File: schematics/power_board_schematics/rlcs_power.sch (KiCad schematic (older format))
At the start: 40 parts, among them J1 SD_Card, J2 Conn_01x05_Male, J3 Conn_01x05_Male, J4 Battery Conn, J5 CONN_01X02, J6 CONN_01X02, J7 CONN_01X02, Q1 Q_NPN_BEC, Q2 Q_NPN_BEC, T1 12 to 3v3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

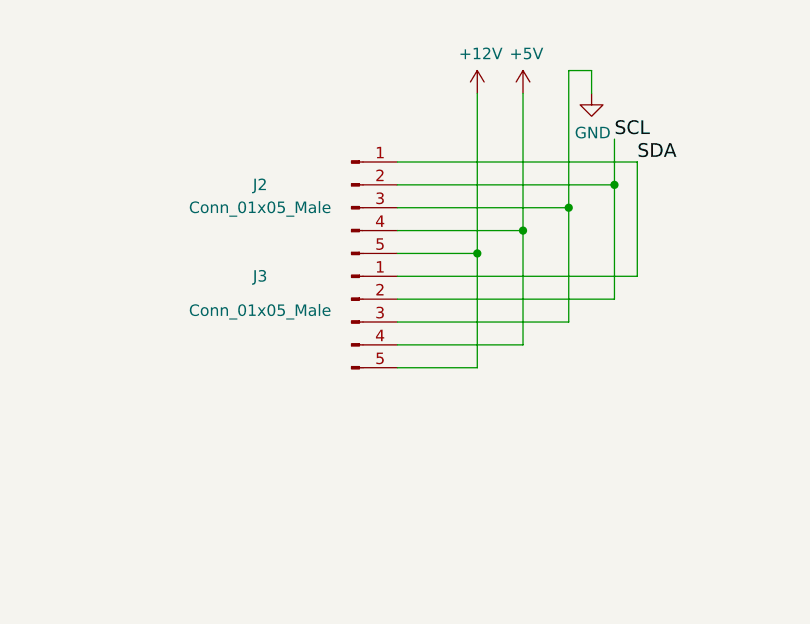
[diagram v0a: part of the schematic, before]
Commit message: Fix 7 segement display pins to make routing easier and fix footprints
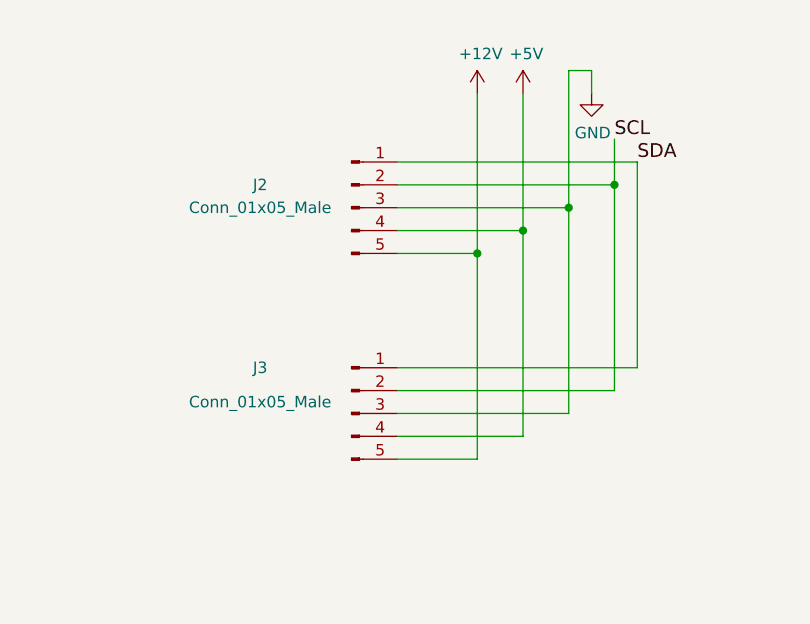
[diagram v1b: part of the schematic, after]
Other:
- moved on the sheet: J3
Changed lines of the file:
@@
 EESchema Schematic File Version 4
-LIBS:rlcs_power-cache
 EELAYER 30 0
 EELAYER END
@@
 Wire Wire Line
 	2650 5850 2500 5850
-Wire Wire Line
-	7750 4750 7750 5250
 Text Label 7750 4750 0    60   ~ 0
 SDA
@@
 Wire Wire Line
 	7550 4350 7550 4450
-Wire Wire Line
-	7650 4850 7650 5350
-Wire Wire Line
-	7750 5250 6700 5250
 Connection ~ 7450 4950
-Wire Wire Line
-	7450 4950 7450 5450
 Connection ~ 7250 5050
 Wire Wire Line
-	7250 5050 7250 5550
-Connection ~ 7050 5150
-Wire Wire Line
-	7050 5150 7050 5650
-Wire Wire Line
 	6700 4750 7750 4750
 Wire Wire Line
@@
 	7450 4350 7550 4350
 Wire Wire Line
-	7050 5650 6700 5650
-Wire Wire Line
-	7250 5550 6700 5550
-Wire Wire Line
-	7450 5450 6700 5450
-Wire Wire Line
-	7650 5350 6700 5350
+	7050 6050 6700 6050
+Wire Wire Line
+	7250 5950 6700 5950
+Wire Wire Line
+	7450 5850 6700 5850
+Wire Wire Line
+	7650 5750 6700 5750
 Connection ~ 7650 4850
 Wire Wire Line
@@
 L Connector:Conn_01x05_Male J3
 U 1 1 5EE7917B
-P 6500 5450
-F 0 "J3" H 6100 5650 50  0000 C CNN
-F 1 "Conn_01x05_Male" H 6100 5500 50  0000 C CNN
-F 2 "Connector_JST:JST_EH_B5B-EH-A_1x05_P2.50mm_Vertical" H 6500 5450 50  0001 C CNN
-F 3 "~" H 6500 5450 50  0001 C CNN
-	1    6500 5450
+P 6500 5850
+F 0 "J3" H 6100 6050 50  0000 C CNN
+F 1 "Conn_01x05_Male" H 6100 5900 50  0000 C CNN
+F 2 "Connector_JST:JST_EH_B5B-EH-A_1x05_P2.50mm_Vertical" H 6500 5850 50  0001 C CNN
+F 3 "~" H 6500 5850 50  0001 C CNN
+	1    6500 5850
 	1    0    0    -1
 $EndComp
@@
 	1    0    0    -1
 $EndComp
+Wire Wire Line
+	6700 5650 7750 5650
+Wire Wire Line
+	7050 5150 7050 6050
+Connection ~ 7050 5150
+Wire Wire Line
+	7250 5050 7250 5950
+Wire Wire Line
+	7450 4950 7450 5850
+Wire Wire Line
+	7650 4850 7650 5750
+Wire Wire Line
+	7750 4750 7750 5650
 $EndSCHEMATC

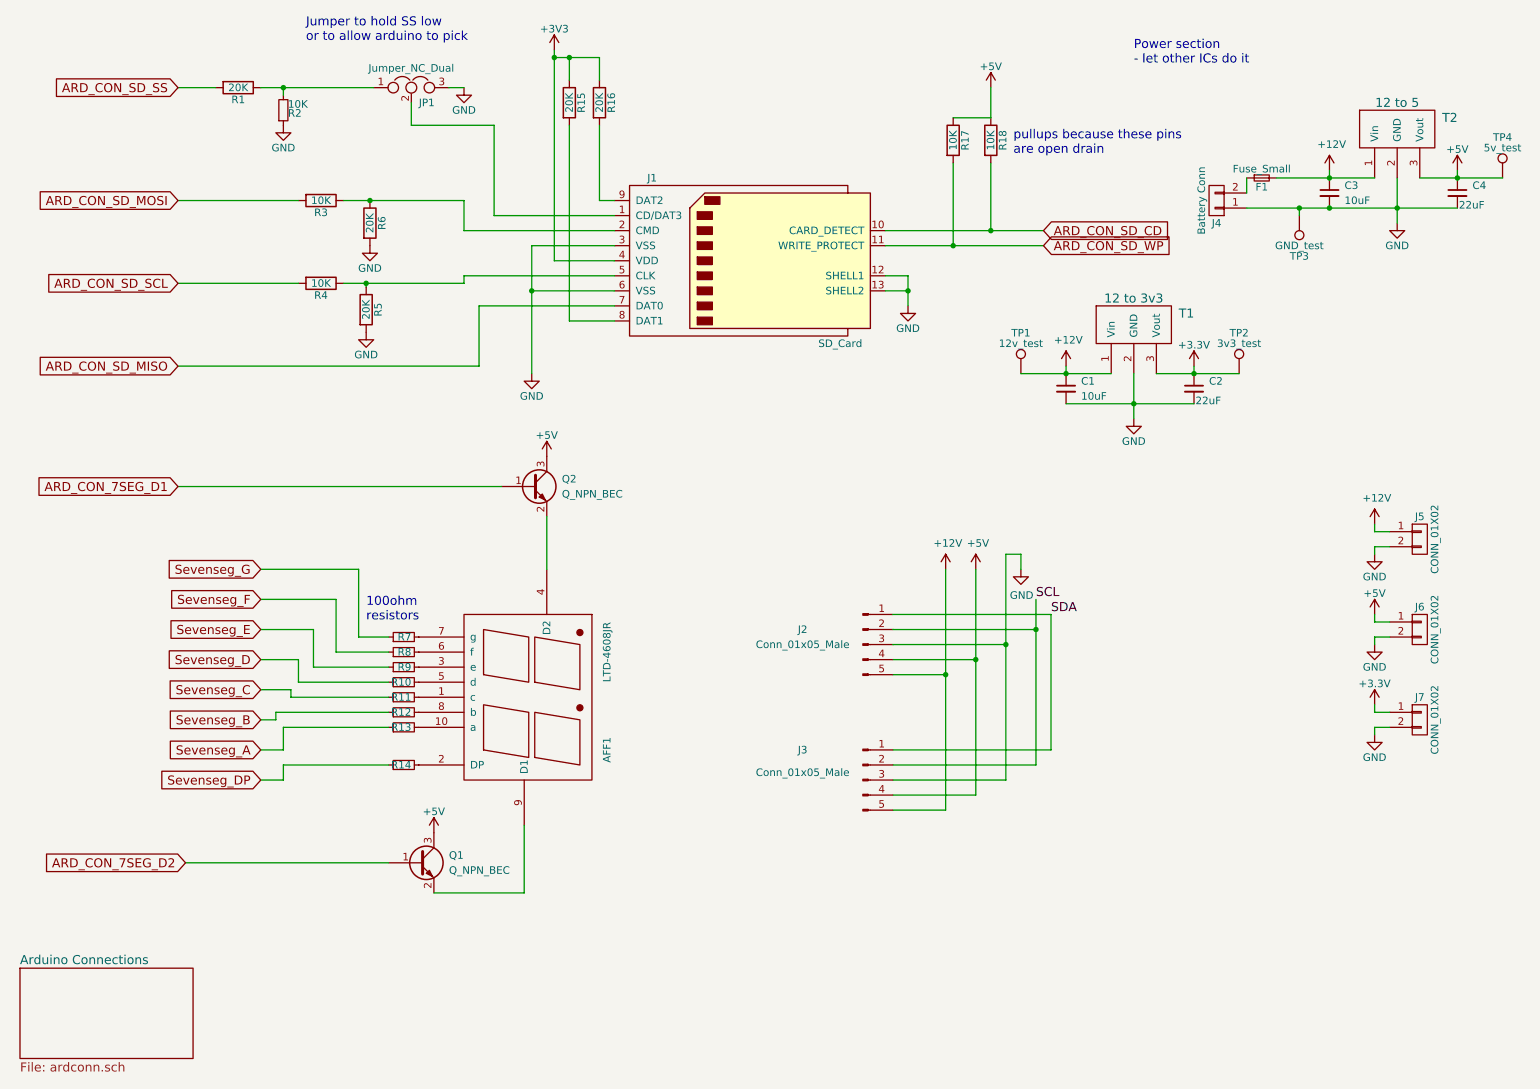
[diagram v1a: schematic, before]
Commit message: Update component placement
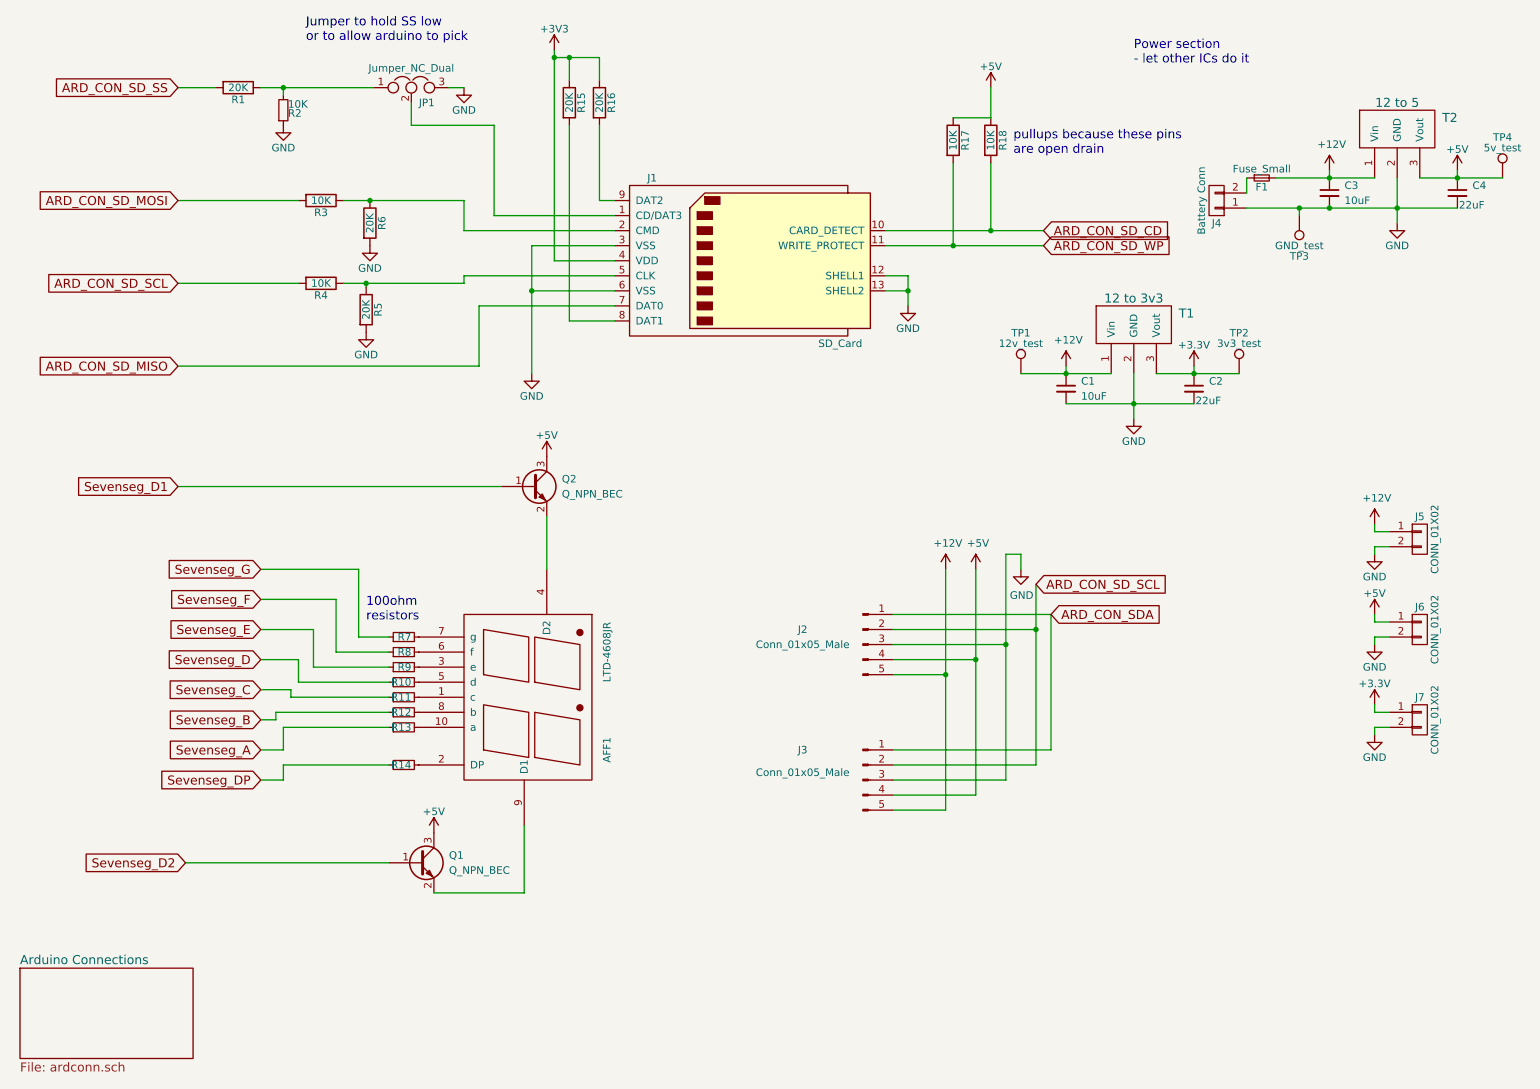
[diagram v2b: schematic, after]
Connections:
- net SCL is gone; now on net ARD_CON_SD_SCL: J2.2 (Pin_2), J3.2 (Pin_2)
- net ARD_CON_7SEG_D1 renamed Sevenseg_D1
- net ARD_CON_7SEG_D2 renamed Sevenseg_D2
- net SDA renamed ARD_CON_SDA
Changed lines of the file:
@@
 $EndComp
 Text GLabel 2000 6400 0    60   Input ~ 0
-ARD_CON_7SEG_D2
+Sevenseg_D2
 $Comp
 L Device:R_Small R14
@@
 $EndComp
 Text GLabel 1950 3900 0    60   Input ~ 0
-ARD_CON_7SEG_D1
+Sevenseg_D1
 $Comp
 L power:+12V #PWR018
@@
 Wire Wire Line
 	2650 5850 2500 5850
-Text Label 7750 4750 0    60   ~ 0
-SDA
-Text Label 7650 4650 0    60   ~ 0
-SCL
 Wire Wire Line
 	7550 4350 7550 4450
@@
 	7650 5750 6700 5750
 Connection ~ 7650 4850
-Wire Wire Line
-	7650 4850 7650 4650
 $Comp
 L Connector:Conn_01x05_Male J3
@@
 Wire Wire Line
 	7750 4750 7750 5650
+Text GLabel 7750 4750 2    60   Input ~ 0
+ARD_CON_SDA
+Wire Wire Line
+	7650 4550 7650 4850
+Text GLabel 7650 4550 2    60   Input ~ 0
+ARD_CON_SD_SCL
 $EndSCHEMATC

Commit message: Address Zach comments
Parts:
- added R19, R20: 4.7K, Resistor_SMD:R_0805_2012Metric_Pad1.15x1.40mm_HandSolder, symbol Device:R
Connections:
- net +5V: now also R19.1, R20.1
- net ARD_CON_SDA: now also R19.2
- net ARD_CON_SD_SCL renamed ARD_CON_SCL
- net ARD_CON_SCL: now also R20.2; no longer R4.2
- new net ARD_CON_SD_SCK: R4.2
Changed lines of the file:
@@
 ARD_CON_SD_MOSI
 Text GLabel 1950 2550 0    60   Input ~ 0
-ARD_CON_SD_SCL
+ARD_CON_SD_SCK
 Text GLabel 1950 3100 0    60   Input ~ 0
 ARD_CON_SD_MISO
@@
 Wire Wire Line
 	7750 4750 7750 5650
-Text GLabel 7750 4750 2    60   Input ~ 0
+Text GLabel 8300 4750 2    60   Input ~ 0
 ARD_CON_SDA
 Wire Wire Line
 	7650 4550 7650 4850
-Text GLabel 7650 4550 2    60   Input ~ 0
-ARD_CON_SD_SCL
+Text GLabel 8250 4550 2    60   Input ~ 0
+ARD_CON_SCL
+$Comp
+L Device:R R19
+U 1 1 602B831C
+P 7750 4300
+F 0 "R19" H 7820 4346 50  0000 L CNN
+F 1 "4.7K" H 7820 4255 50  0000 L CNN
+F 2 "Resistor_SMD:R_0805_2012Metric_Pad1.15x1.40mm_HandSolder" V 7680 4300 50  0001 C CNN
+F 3 "~" H 7750 4300 50  0001 C CNN
+	1    7750 4300
+	1    0    0    -1
+$EndComp
+$Comp
+L Device:R R20
+U 1 1 602B8F94
+P 8050 4300
+F 0 "R20" H 8120 4346 50  0000 L CNN
+F 1 "4.7K" H 8120 4255 50  0000 L CNN
+F 2 "Resistor_SMD:R_0805_2012Metric_Pad1.15x1.40mm_HandSolder" V 7980 4300 50  0001 C CNN
+F 3 "~" H 8050 4300 50  0001 C CNN
+	1    8050 4300
+	1    0    0    -1
+$EndComp
+$Comp
+L power:+5V #PWR0101
+U 1 1 602B9A36
+P 7750 4150
+F 0 "#PWR0101" H 7750 4000 50  0001 C CNN
+F 1 "+5V" H 7765 4323 50  0000 C CNN
+F 2 "" H 7750 4150 50  0001 C CNN
+F 3 "" H 7750 4150 50  0001 C CNN
+	1    7750 4150
+	1    0    0    -1
+$EndComp
+$Comp
+L power:+5V #PWR0102
+U 1 1 602BA28A
+P 8050 4150
+F 0 "#PWR0102" H 8050 4000 50  0001 C CNN
+F 1 "+5V" H 8065 4323 50  0000 C CNN
+F 2 "" H 8050 4150 50  0001 C CNN
+F 3 "" H 8050 4150 50  0001 C CNN
+	1    8050 4150
+	1    0    0    -1
+$EndComp
+Wire Wire Line
+	8250 4550 8050 4550
+Wire Wire Line
+	8050 4450 8050 4550
+Connection ~ 8050 4550
+Wire Wire Line
+	8050 4550 7650 4550
+Wire Wire Line
+	8300 4750 7750 4750
+Connection ~ 7750 4750
+Wire Wire Line
+	7750 4450 7750 4750
 $EndSCHEMATC

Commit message: Update footprint resistors
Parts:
- R1, R10, R11, R12, R13, R14, R15, R16, R17, R18, R19, R2, R20, R3, R4, R5, R6, R7, R8, R9: footprint Resistor_SMD:R_0805_2012Metric_Pad1.15x1.40mm_HandSolder -> Resistor_SMD:R_0805_2012Metric_Pad1.20x1.40mm_HandSolder
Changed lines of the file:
@@
 F 0 "R2" H 2680 1420 50  0000 L CNN
 F 1 "10K" H 2680 1360 50  0000 L CNN
-F 2 "Resistor_SMD:R_0805_2012Metric_Pad1.15x1.40mm_HandSolder" H 2650 1400 50  0001 C CNN
+F 2 "Resistor_SMD:R_0805_2012Metric_Pad1.20x1.40mm_HandSolder" H 2650 1400 50  0001 C CNN
 F 3 "" H 2650 1400 50  0001 C CNN
 	1    2650 1400
@@
 F 0 "R15" V 4630 1350 50  0000 C CNN
 F 1 "20K" V 4550 1350 50  0000 C CNN
-F 2 "Resistor_SMD:R_0805_2012Metric_Pad1.15x1.40mm_HandSolder" V 4480 1350 50  0001 C CNN
+F 2 "Resistor_SMD:R_0805_2012Metric_Pad1.20x1.40mm_HandSolder" V 4480 1350 50  0001 C CNN
 F 3 "" H 4550 1350 50  0001 C CNN
 	1    4550 1350
@@
 F 0 "R16" V 4830 1350 50  0000 C CNN
 F 1 "20K" V 4750 1350 50  0000 C CNN
-F 2 "Resistor_SMD:R_0805_2012Metric_Pad1.15x1.40mm_HandSolder" V 4680 1350 50  0001 C CNN
+F 2 "Resistor_SMD:R_0805_2012Metric_Pad1.20x1.40mm_HandSolder" V 4680 1350 50  0001 C CNN
 F 3 "" H 4750 1350 50  0001 C CNN
 	1    4750 1350
@@
 F 0 "R18" V 7430 1600 50  0000 C CNN
 F 1 "10K" V 7350 1600 50  0000 C CNN
-F 2 "Resistor_SMD:R_0805_2012Metric_Pad1.15x1.40mm_HandSolder" V 7280 1600 50  0001 C CNN
+F 2 "Resistor_SMD:R_0805_2012Metric_Pad1.20x1.40mm_HandSolder" V 7280 1600 50  0001 C CNN
 F 3 "" H 7350 1600 50  0001 C CNN
 	1    7350 1600
@@
 F 0 "R17" V 7180 1600 50  0000 C CNN
 F 1 "10K" V 7100 1600 50  0000 C CNN
-F 2 "Resistor_SMD:R_0805_2012Metric_Pad1.15x1.40mm_HandSolder" V 7030 1600 50  0001 C CNN
+F 2 "Resistor_SMD:R_0805_2012Metric_Pad1.20x1.40mm_HandSolder" V 7030 1600 50  0001 C CNN
 F 3 "" H 7100 1600 50  0001 C CNN
 	1    7100 1600
@@
 F 0 "R1" V 2430 1250 50  0000 C CNN
 F 1 "20K" V 2350 1250 50  0000 C CNN
-F 2 "Resistor_SMD:R_0805_2012Metric_Pad1.15x1.40mm_HandSolder" V 2280 1250 50  0001 C CNN
+F 2 "Resistor_SMD:R_0805_2012Metric_Pad1.20x1.40mm_HandSolder" V 2280 1250 50  0001 C CNN
 F 3 "" H 2350 1250 50  0001 C CNN
 	1    2350 1250
@@
 F 0 "R6" V 3305 2150 50  0000 C CNN
 F 1 "20K" V 3225 2150 50  0000 C CNN
-F 2 "Resistor_SMD:R_0805_2012Metric_Pad1.15x1.40mm_HandSolder" V 3155 2150 50  0001 C CNN
+F 2 "Resistor_SMD:R_0805_2012Metric_Pad1.20x1.40mm_HandSolder" V 3155 2150 50  0001 C CNN
 F 3 "" H 3225 2150 50  0001 C CNN
 	1    3225 2150
@@
 F 0 "R5" V 3280 2725 50  0000 C CNN
 F 1 "20K" V 3200 2725 50  0000 C CNN
-F 2 "Resistor_SMD:R_0805_2012Metric_Pad1.15x1.40mm_HandSolder" V 3130 2725 50  0001 C CNN
+F 2 "Resistor_SMD:R_0805_2012Metric_Pad1.20x1.40mm_HandSolder" V 3130 2725 50  0001 C CNN
 F 3 "" H 3200 2725 50  0001 C CNN
 	1    3200 2725
@@
 F 0 "R3" V 2980 2000 50  0000 C CNN
 F 1 "10K" V 2900 2000 50  0000 C CNN
-F 2 "Resistor_SMD:R_0805_2012Metric_Pad1.15x1.40mm_HandSolder" V 2830 2000 50  0001 C CNN
+F 2 "Resistor_SMD:R_0805_2012Metric_Pad1.20x1.40mm_HandSolder" V 2830 2000 50  0001 C CNN
 F 3 "" H 2900 2000 50  0001 C CNN
 	1    2900 2000
@@
 F 0 "R4" V 2980 2550 50  0000 C CNN
 F 1 "10K" V 2900 2550 50  0000 C CNN
-F 2 "Resistor_SMD:R_0805_2012Metric_Pad1.15x1.40mm_HandSolder" V 2830 2550 50  0001 C CNN
+F 2 "Resistor_SMD:R_0805_2012Metric_Pad1.20x1.40mm_HandSolder" V 2830 2550 50  0001 C CNN
 F 3 "" H 2900 2550 50  0001 C CNN
 	1    2900 2550
@@
 F 0 "R14" V 3450 5700 50  0000 L CNN
 F 1 "150" V 3500 5700 50  0001 L CNN
-F 2 "Resistor_SMD:R_0805_2012Metric_Pad1.15x1.40mm_HandSolder" H 3450 5750 50  0001 C CNN
+F 2 "Resistor_SMD:R_0805_2012Metric_Pad1.20x1.40mm_HandSolder" H 3450 5750 50  0001 C CNN
 F 3 "" H 3450 5750 50  0001 C CNN
 	1    3450 5750
@@
 F 0 "R13" V 3450 5450 50  0000 L CNN
 F 1 "150" V 3500 5450 50  0001 L CNN
-F 2 "Resistor_SMD:R_0805_2012Metric_Pad1.15x1.40mm_HandSolder" H 3450 5500 50  0001 C CNN
+F 2 "Resistor_SMD:R_0805_2012Metric_Pad1.20x1.40mm_HandSolder" H 3450 5500 50  0001 C CNN
 F 3 "" H 3450 5500 50  0001 C CNN
 	1    3450 5500
@@
 F 0 "R12" V 3450 5350 50  0000 L CNN
 F 1 "150" V 3500 5350 50  0001 L CNN
-F 2 "Resistor_SMD:R_0805_2012Metric_Pad1.15x1.40mm_HandSolder" H 3450 5400 50  0001 C CNN
+F 2 "Resistor_SMD:R_0805_2012Metric_Pad1.20x1.40mm_HandSolder" H 3450 5400 50  0001 C CNN
 F 3 "" H 3450 5400 50  0001 C CNN
 	1    3450 5400
@@
 F 0 "R11" V 3450 5250 50  0000 L CNN
 F 1 "150" V 3500 5250 50  0001 L CNN
-F 2 "Resistor_SMD:R_0805_2012Metric_Pad1.15x1.40mm_HandSolder" H 3450 5300 50  0001 C CNN
+F 2 "Resistor_SMD:R_0805_2012Metric_Pad1.20x1.40mm_HandSolder" H 3450 5300 50  0001 C CNN
 F 3 "" H 3450 5300 50  0001 C CNN
 	1    3450 5300
@@
 F 0 "R10" V 3450 5150 50  0000 L CNN
 F 1 "150" V 3500 5150 50  0001 L CNN
-F 2 "Resistor_SMD:R_0805_2012Metric_Pad1.15x1.40mm_HandSolder" H 3450 5200 50  0001 C CNN
+F 2 "Resistor_SMD:R_0805_2012Metric_Pad1.20x1.40mm_HandSolder" H 3450 5200 50  0001 C CNN
 F 3 "" H 3450 5200 50  0001 C CNN
 	1    3450 5200
@@
 F 0 "R9" V 3450 5050 50  0000 L CNN
 F 1 "150" V 3500 5050 50  0001 L CNN
-F 2 "Resistor_SMD:R_0805_2012Metric_Pad1.15x1.40mm_HandSolder" H 3450 5100 50  0001 C CNN
+F 2 "Resistor_SMD:R_0805_2012Metric_Pad1.20x1.40mm_HandSolder" H 3450 5100 50  0001 C CNN
 F 3 "" H 3450 5100 50  0001 C CNN
 	1    3450 5100
@@
 F 0 "R8" V 3450 4950 50  0000 L CNN
 F 1 "150" V 3500 4950 50  0001 L CNN
-F 2 "Resistor_SMD:R_0805_2012Metric_Pad1.15x1.40mm_HandSolder" H 3450 5000 50  0001 C CNN
+F 2 "Resistor_SMD:R_0805_2012Metric_Pad1.20x1.40mm_HandSolder" H 3450 5000 50  0001 C CNN
 F 3 "" H 3450 5000 50  0001 C CNN
 	1    3450 5000
@@
 F 0 "R7" V 3450 4850 50  0000 L CNN
 F 1 "150" V 3500 4850 50  0001 L CNN
-F 2 "Resistor_SMD:R_0805_2012Metric_Pad1.15x1.40mm_HandSolder" H 3450 4900 50  0001 C CNN
+F 2 "Resistor_SMD:R_0805_2012Metric_Pad1.20x1.40mm_HandSolder" H 3450 4900 50  0001 C CNN
 F 3 "" H 3450 4900 50  0001 C CNN
 	1    3450 4900
@@
 F 0 "R19" H 7820 4346 50  0000 L CNN
 F 1 "4.7K" H 7820 4255 50  0000 L CNN
-F 2 "Resistor_SMD:R_0805_2012Metric_Pad1.15x1.40mm_HandSolder" V 7680 4300 50  0001 C CNN
+F 2 "Resistor_SMD:R_0805_2012Metric_Pad1.20x1.40mm_HandSolder" V 7680 4300 50  0001 C CNN
 F 3 "~" H 7750 4300 50  0001 C CNN
 	1    7750 4300
@@
 F 0 "R20" H 8120 4346 50  0000 L CNN
 F 1 "4.7K" H 8120 4255 50  0000 L CNN
-F 2 "Resistor_SMD:R_0805_2012Metric_Pad1.15x1.40mm_HandSolder" V 7980 4300 50  0001 C CNN
+F 2 "Resistor_SMD:R_0805_2012Metric_Pad1.20x1.40mm_HandSolder" V 7980 4300 50  0001 C CNN
 F 3 "~" H 8050 4300 50  0001 C CNN
 	1    8050 4300
